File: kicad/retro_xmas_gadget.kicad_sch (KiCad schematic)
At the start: 75 parts, among them J1 USB_C_Receptacle_USB2.0_16P, J2 SD_Card_Receptacle, J3 AudioJack3_SwitchTR, J4 Conn_01x18, J5 Conn_01x02, J6 Conn_01x03, J7 Conn_01x03, J8 Conn_01x07, Q1 UMH3N, Q2 SS8050, SW1 RESET, SW10 SELECT, SW11 START, SW12 A, SW13 B, SW2 BOOT, SW3 KH-SS12F23-G6, SW4 UP, SW5 DOWN, SW6 LEFT, SW7 RIGHT, SW8 MENU, SW9 OPTION, U1 CP2102N-Axx-xQFN28, U2 ESP32-S3-WROOM-1, U4 XC6210B332MR, U5 TP4056

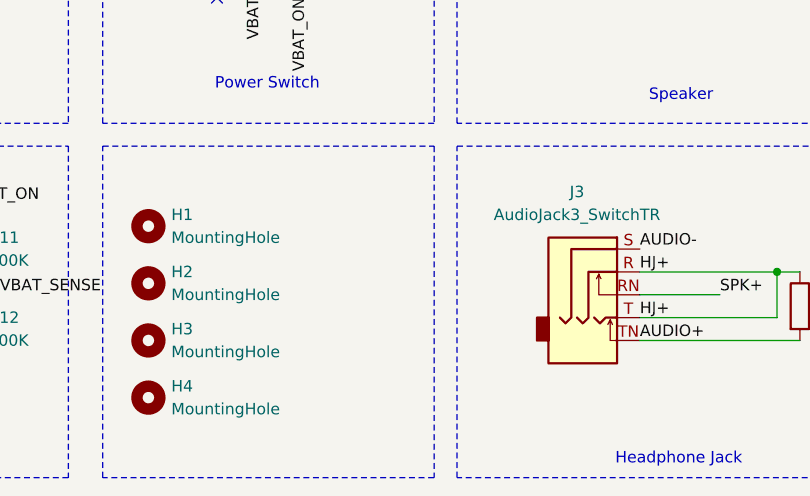
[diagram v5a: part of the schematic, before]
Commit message: adjustments with 3d model
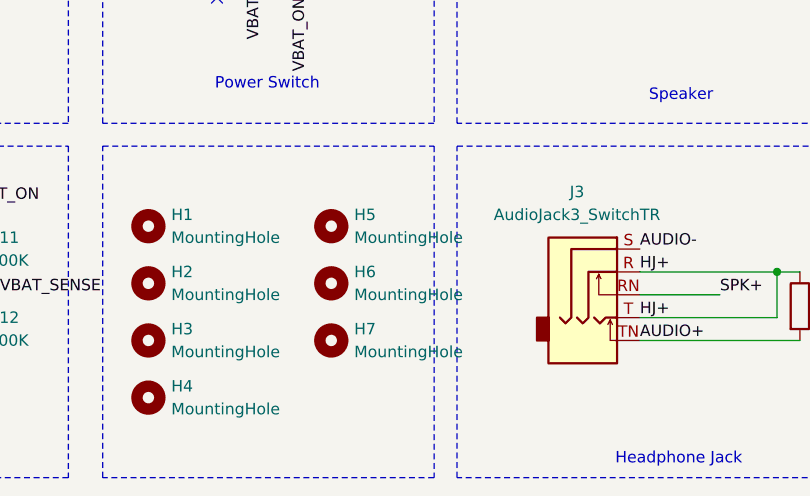
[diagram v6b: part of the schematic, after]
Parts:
- added H5, H6, H7: MountingHole, MountingHole:MountingHole_2.5mm, symbol Mechanical:MountingHole
- H1: footprint MountingHole:MountingHole_2.7mm_M2.5 -> MountingHole:MountingHole_4.3mm_M4
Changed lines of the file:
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@@
 	)
 	(symbol
+		(lib_id "Mechanical:MountingHole")
+		(at 80.01 257.81 0)
+		(unit 1)
+		(exclude_from_sim yes)
+		(in_bom no)
+		(on_board yes)
+		(dnp no)
+		(fields_autoplaced yes)
+		(property "Reference" "H7"
+			(at 82.55 256.5399 0)
+			(effects
+				(font
+					(size 1.27 1.27)
+				)
+				(justify left)
+			)
+		)
+		(property "Value" "MountingHole"
+			(at 82.55 259.0799 0)
+			(effects
+				(font
+					(size 1.27 1.27)
+				)
+				(justify left)
+			)
+		)
+		(property "Footprint" "MountingHole:MountingHole_2.5mm"
+			(at 80.01 257.81 0)
+			(effects
+				(font
+					(size 1.27 1.27)
+				)
+				(hide yes)
+			)
+		)
+		(property "Datasheet" "~"
+			(at 80.01 257.81 0)
+			(effects
+				(font
+					(size 1.27 1.27)
+				)
+				(hide yes)
+			)
+		)
+		(property "Description" "Mounting Hole without connection"
+			(at 80.01 257.81 0)
+			(effects
+				(font
+					(size 1.27 1.27)
+				)
+				(hide yes)
+			)
+		)
+		(instances
+			(project "retro_xmas_gadget"
+				(path "/7dc616d3-242c-452f-9b6f-7840adb01747"
+					(reference "H7")
+					(unit 1)
+				)
+			)
+		)
+	)
+	(symbol
 		(lib_id "Switch:SW_Push")
 		(at 300.99 175.26 0)
@@
 	)
 	(symbol
+		(lib_id "Mechanical:MountingHole")
+		(at 80.01 251.46 0)
+		(unit 1)
+		(exclude_from_sim yes)
+		(in_bom no)
+		(on_board yes)
+		(dnp no)
+		(fields_autoplaced yes)
+		(property "Reference" "H6"
+			(at 82.55 250.1899 0)
+			(effects
+				(font
+					(size 1.27 1.27)
+				)
+				(justify left)
+			)
+		)
+		(property "Value" "MountingHole"
+			(at 82.55 252.7299 0)
+			(effects
+				(font
+					(size 1.27 1.27)
+				)
+				(justify left)
+			)
+		)
+		(property "Footprint" "MountingHole:MountingHole_2.5mm"
+			(at 80.01 251.46 0)
+			(effects
+				(font
+					(size 1.27 1.27)
+				)
+				(hide yes)
+			)
+		)
+		(property "Datasheet" "~"
+			(at 80.01 251.46 0)
+			(effects
+				(font
+					(size 1.27 1.27)
+				)
+				(hide yes)
+			)
+		)
+		(property "Description" "Mounting Hole without connection"
+			(at 80.01 251.46 0)
+			(effects
+				(font
+					(size 1.27 1.27)
+				)
+				(hide yes)
+			)
+		)
+		(instances
+			(project "retro_xmas_gadget"
+				(path "/7dc616d3-242c-452f-9b6f-7840adb01747"
+					(reference "H6")
+					(unit 1)
+				)
+			)
+		)
+	)
+	(symbol
 		(lib_id "power:VAA")
 		(at 118.11 120.65 0)
@@
 	)
 	(symbol
+		(lib_id "Mechanical:MountingHole")
+		(at 80.01 245.11 0)
+		(unit 1)
+		(exclude_from_sim yes)
+		(in_bom no)
+		(on_board yes)
+		(dnp no)
+		(fields_autoplaced yes)
+		(property "Reference" "H5"
+			(at 82.55 243.8399 0)
+			(effects
+				(font
+					(size 1.27 1.27)
+				)
+				(justify left)
+			)
+		)
+		(property "Value" "MountingHole"
+			(at 82.55 246.3799 0)
+			(effects
+				(font
+					(size 1.27 1.27)
+				)
+				(justify left)
+			)
+		)
+		(property "Footprint" "MountingHole:MountingHole_2.5mm"
+			(at 80.01 245.11 0)
+			(effects
+				(font
+					(size 1.27 1.27)
+				)
+				(hide yes)
+			)
+		)
+		(property "Datasheet" "~"
+			(at 80.01 245.11 0)
+			(effects
+				(font
+					(size 1.27 1.27)
+				)
+				(hide yes)
+			)
+		)
+		(property "Description" "Mounting Hole without connection"
+			(at 80.01 245.11 0)
+			(effects
+				(font
+					(size 1.27 1.27)
+				)
+				(hide yes)
+			)
+		)
+		(instances
+			(project "retro_xmas_gadget"
+				(path "/7dc616d3-242c-452f-9b6f-7840adb01747"
+					(reference "H5")
+					(unit 1)
+				)
+			)
+		)
+	)
+	(symbol
 		(lib_id "Device:C")
 		(at 194.31 143.51 0)
@@
 			)
 		)
-		(property "Footprint" "MountingHole:MountingHole_2.7mm_M2.5"
+		(property "Footprint" "MountingHole:MountingHole_4.3mm_M4"
 			(at 59.69 245.11 0)
 			(effects

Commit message: mayor checks
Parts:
- removed R17: 0, Capacitor_SMD:C_0402_1005Metric, symbol Device:R
- H1: footprint MountingHole:MountingHole_4.3mm_M4 -> MountingHole:MountingHole_2.7mm_M2.5
- H7: footprint MountingHole:MountingHole_2.5mm -> MountingHole:MountingHole_4.3mm_M4
- R20: footprint (none) -> Resistor_SMD:R_0603_1608Metric_Pad0.98x0.95mm_HandSolder
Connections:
- net VBAT: now also J6.1 (Pin_1)
- net VBAT_ON: no longer J6.1 (Pin_1)
- net VBUS: now also U1.7 (VREGIN)
- no-connect marks 19 -> 35
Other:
- note added: "Check where EP's should be connected"
- note added: "Mounting hole sizes"
- note removed: "Check CP2102"
- note removed: "Check headphone jack"
- note removed: "Labels for BOOT, RESET"
- moved on the sheet: C1, C2, C3, C4, R3, R4

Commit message: almost complete
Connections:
- net GND: no longer U5.1 (TEMP)
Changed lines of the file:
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@@
-	)
-	(junction
-		(at 20.32 147.32)
-		(diameter 0)
-		(color 0 0 0 0)
 	)
 	(junction
@@
 	(wire
 		(pts
-			(xy 17.78 127) (xy 17.78 147.32)
-		)
-		(stroke
-			(width 0)
-			(type default)
-		)
-	)
-	(wire
-		(pts
 			(xy 39.37 147.32) (xy 55.88 147.32)
 		)
@@
 	(wire
 		(pts
-			(xy 17.78 147.32) (xy 20.32 147.32)
-		)
-		(stroke
-			(width 0)
-			(type default)
-		)
-	)
-	(wire
-		(pts
 			(xy 60.96 33.02) (xy 60.96 29.21)
 		)
@@
 		)
 		(stroke
-			(width 0)
-			(type default)
-		)
-	)
-	(wire
-		(pts
-			(xy 24.13 127) (xy 17.78 127)
-		)
-		(stroke
